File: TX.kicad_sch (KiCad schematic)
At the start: 0 parts

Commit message: Added some little bits and bops
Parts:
- added Q2, Q5: MJD44H11T4G, BR_SOT:TO-252-2_L6.5-W6.1-P4.58-LS10.0-TL, symbol BR_Transistors:BJT_N_MJD44H11T4G
- added Q3, Q4: MJD45H11T4G, BR_SOT:TO-252-2_L6.5-W6.1-P4.58-LS10.0-TL, symbol BR_Transistors:BJT_P_MJD45H11T4G

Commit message: Update TX.kicad_sch
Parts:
- removed Q4: MJD45H11T4G, BR_SOT:TO-252-2_L6.5-W6.1-P4.58-LS10.0-TL, symbol BR_Transistors:BJT_P_MJD45H11T4G
- removed Q5: MJD44H11T4G, BR_SOT:TO-252-2_L6.5-W6.1-P4.58-LS10.0-TL, symbol BR_Transistors:BJT_N_MJD44H11T4G
- Q2: JLCPCB Part Num (none) -> C38780
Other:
- note added: "For collector currents < 1A, these FETs have a current-gain-BW product of around 90MHz For 1A output, we'd need op-amps that can source 10mA"
- note added: "The biasing op amp (using output feedback) needs to have an Enable pin. We want the op amp to enter a high-Z state when not transmitting to avoid driving the BJTs and letting the 1k resistor pull the BJTs off."
- moved on the sheet: Q2, Q3

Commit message: power scheme
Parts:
- added Q4: MJD45H11T4G, BR_SOT:TO-252-2_L6.5-W6.1-P4.58-LS10.0-TL, symbol BR_Transistors:BJT_P_MJD45H11T4G
- added Q5: MJD44H11T4G, BR_SOT:TO-252-2_L6.5-W6.1-P4.58-LS10.0-TL, symbol BR_Transistors:BJT_N_MJD44H11T4G
- Q2: JLCPCB Part Num C38780 -> (none)
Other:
- note removed: "For collector currents < 1A, these FETs have a current-gain-BW product of around 90MHz For 1A output, we'd need op-amps that can source 10mA"
- note removed: "The biasing op amp (using output feedback) needs to have an Enable pin. We want the op amp to enter a high-Z state when not transmitting to avoid driving the BJTs and letting the 1k resistor pull the BJTs off."
- moved on the sheet: Q2, Q3

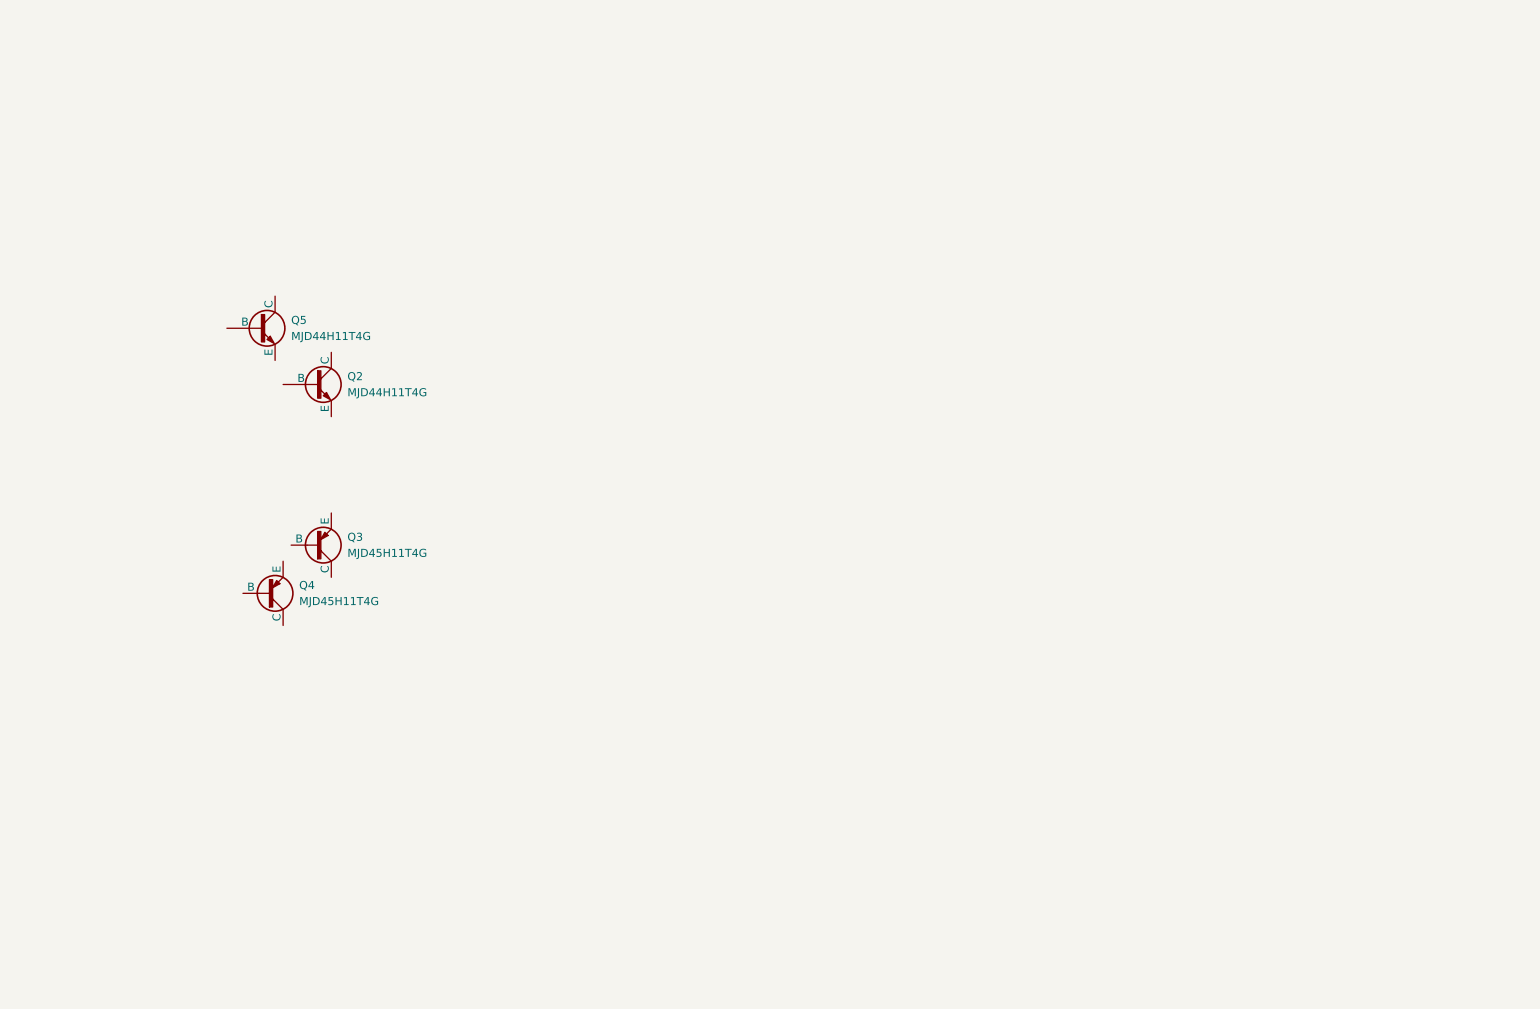
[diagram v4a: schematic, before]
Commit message: Added integrated class ab
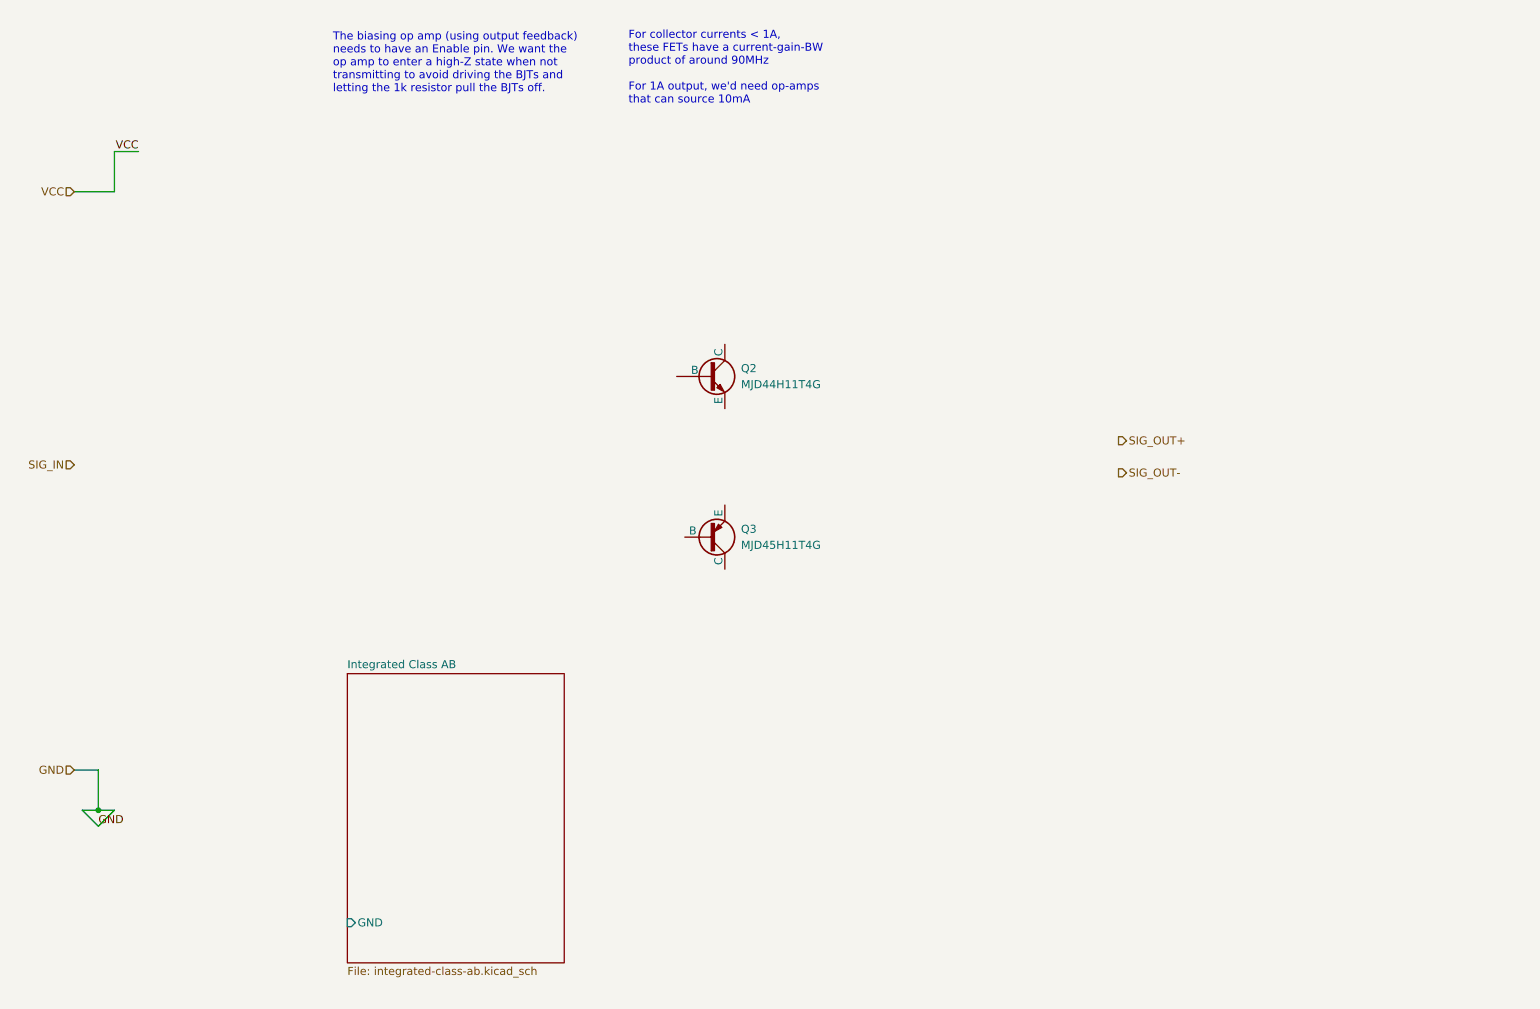
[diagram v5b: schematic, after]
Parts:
- removed Q4: MJD45H11T4G, BR_SOT:TO-252-2_L6.5-W6.1-P4.58-LS10.0-TL, symbol BR_Transistors:BJT_P_MJD45H11T4G
- removed Q5: MJD44H11T4G, BR_SOT:TO-252-2_L6.5-W6.1-P4.58-LS10.0-TL, symbol BR_Transistors:BJT_N_MJD44H11T4G
- Q2: JLCPCB Part Num (none) -> C38780
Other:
- added sheet Integrated Class AB (integrated-class-ab.kicad_sch)
- note added: "For collector currents < 1A, these FETs have a current-gain-BW product of around 90MHz For 1A output, we'd need op-amps that can source 10mA"
- note added: "The biasing op amp (using output feedback) needs to have an Enable pin. We want the op amp to enter a high-Z state when not transmitting to avoid driving the BJTs and letting the 1k resistor pull the BJTs off."
- moved on the sheet: Q2, Q3

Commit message: Added the pin headers to TX, working on a HV line driver design
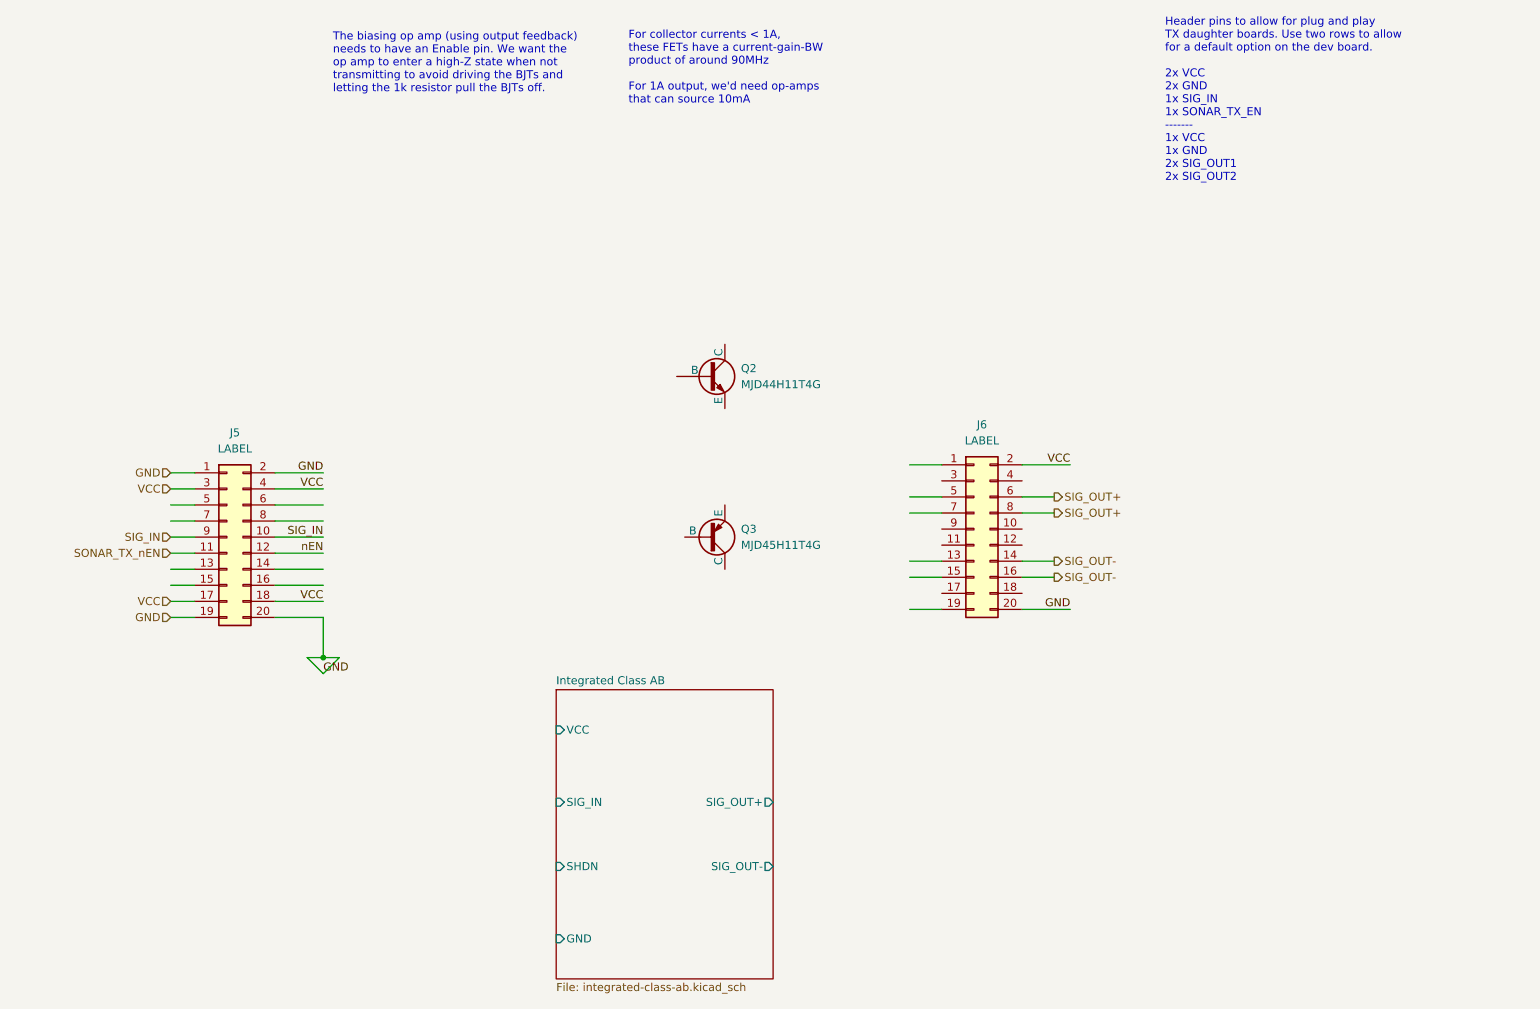
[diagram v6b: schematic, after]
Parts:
- added J5, J6: LABEL, BR_Connectors:HDR-SMD_20P-P2.54-V-M-R2-C10-S7.5, symbol BR_Connectors_Header:Header_Pin_02x10_2.54mm_Vert_PTH
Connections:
- net GND: now also J5.1 (Pin_1), J5.19 (Pin_19), J5.2 (Pin_2), J5.20 (Pin_20), J6.20 (Pin_20)
- net SIG_IN: now also J5.10 (Pin_10), J5.9 (Pin_9)
- net SIG_OUT+: now also J6.6 (Pin_6), J6.8 (Pin_8)
- net SIG_OUT-: now also J6.14 (Pin_14), J6.16 (Pin_16)
- net VCC: now also J5.17 (Pin_17), J5.18 (Pin_18), J5.3 (Pin_3), J5.4 (Pin_4), J6.2 (Pin_2)
- new net SONAR_TX_nEN: J5.11 (Pin_11)
- new net nEN: J5.12 (Pin_12)
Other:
- sheet Integrated Class AB ports: added SHDN, SIG_IN, SIG_OUT+, SIG_OUT-, VCC; removed none
- note added: "Header pins to allow for plug and play TX daughter boards. Use two rows to allow for a default option on the dev board. 2x VCC 2x GND 1x SIG_IN 1x SONAR_TX_EN ------- 1x VCC 1x GND 2x SIG_OUT1 2x SIG_OUT2"

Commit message: Created DAC single-ended to double-ended pre stage for TX path
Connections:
- net 4V: now reaches J5.5 (Pin_5)
- net 4V: now also J5.6 (Pin_6)
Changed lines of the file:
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@@
 		(color 0 0 0 0)
 	)
+	(junction
+		(at 128.27 166.37)
+		(diameter 0)
+		(color 0 0 0 0)
+	)
 	(wire
 		(pts
@@
 	(wire
 		(pts
+			(xy 128.27 127) (xy 128.27 119.38)
+		)
+		(stroke
+			(width 0)
+			(type default)
+		)
+	)
+	(wire
+		(pts
 			(xy 99.06 109.22) (xy 99.06 115.57)
 		)
@@
 	(wire
 		(pts
+			(xy 135.89 160.02) (xy 128.27 160.02)
+		)
+		(stroke
+			(width 0)
+			(type default)
+		)
+	)
+	(wire
+		(pts
 			(xy 214.63 102.87) (xy 209.55 102.87)
 		)
@@
 	(wire
 		(pts
+			(xy 124.46 119.38) (xy 128.27 119.38)
+		)
+		(stroke
+			(width 0)
+			(type default)
+		)
+	)
+	(wire
+		(pts
 			(xy 91.44 96.52) (xy 99.06 96.52)
 		)
@@
 	(wire
 		(pts
+			(xy 125.73 148.59) (xy 135.89 148.59)
+		)
+		(stroke
+			(width 0)
+			(type default)
+		)
+	)
+	(wire
+		(pts
 			(xy 91.44 109.22) (xy 99.06 109.22)
 		)
@@
 	(wire
 		(pts
+			(xy 128.27 166.37) (xy 125.73 166.37)
+		)
+		(stroke
+			(width 0)
+			(type default)
+		)
+	)
+	(wire
+		(pts
 			(xy 191.77 90.17) (xy 196.85 90.17)
 		)
@@
 	(wire
 		(pts
+			(xy 135.89 127) (xy 128.27 127)
+		)
+		(stroke
+			(width 0)
+			(type default)
+		)
+	)
+	(wire
+		(pts
+			(xy 128.27 168.91) (xy 125.73 166.37)
+		)
+		(stroke
+			(width 0)
+			(type default)
+		)
+	)
+	(wire
+		(pts
 			(xy 91.44 101.6) (xy 99.06 101.6)
 		)
@@
 	(wire
 		(pts
+			(xy 125.73 138.43) (xy 135.89 138.43)
+		)
+		(stroke
+			(width 0)
+			(type default)
+		)
+	)
+	(wire
+		(pts
 			(xy 91.44 91.44) (xy 99.06 91.44)
 		)
@@
 	(wire
 		(pts
+			(xy 128.27 160.02) (xy 128.27 166.37)
+		)
+		(stroke
+			(width 0)
+			(type default)
+		)
+	)
+	(wire
+		(pts
 			(xy 91.44 93.98) (xy 99.06 93.98)
 		)
@@
 	(wire
 		(pts
+			(xy 130.81 166.37) (xy 128.27 168.91)
+		)
+		(stroke
+			(width 0)
+			(type default)
+		)
+	)
+	(wire
+		(pts
 			(xy 74.93 86.36) (xy 78.74 86.36)
 		)
@@
 		(pts
 			(xy 96.52 115.57) (xy 99.06 115.57)
+		)
+		(stroke
+			(width 0)
+			(type default)
+		)
+	)
+	(wire
+		(pts
+			(xy 130.81 166.37) (xy 128.27 166.37)
 		)
 		(stroke
@@
 		)
 	)
+	(label "4V"
+		(at 99.06 91.44 180)
+		(effects
+			(font
+				(size 1.27 1.27)
+			)
+			(justify right bottom)
+		)
+	)
 	(label "GND"
 		(at 217.17 107.95 180)
@@
 	)
 	(label "VCC"
+		(at 124.46 119.38 0)
+		(effects
+			(font
+				(size 1.27 1.27)
+			)
+			(justify left bottom)
+		)
+	)
+	(label "VCC"
 		(at 99.06 106.68 180)
 		(effects
@@
 	(label "nEN"
 		(at 99.06 99.06 180)
+		(effects
+			(font
+				(size 1.27 1.27)
+			)
+			(justify right bottom)
+		)
+	)
+	(label "GND"
+		(at 128.27 168.91 180)
 		(effects
 			(font
@@
 		(effects
 			(font
+				(size 1.27 1.27)
+			)
+			(justify right)
+		)
+	)
+	(hierarchical_label "4V"
+		(shape input)
+		(at 74.93 91.44 180)
+		(effects
+			(font

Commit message: shit on a shit stick
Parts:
- added R48: 20k, BR_Passives:R_0201_0603Metric-minimized, symbol BR_Resistors_0201:R_0201_20k
- added R49: 2k, BR_Passives:C_0402_1005Metric-minimized, symbol BR_Resistors_0402:R_0402_2k
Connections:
- net SIG_IN: now also R48.1, R49.1
- net 2x_ATT: now reaches J5.14 (Pin_14)
- net 2x_ATT: now also R48.2
- net 10x_ATT: now reaches J5.16 (Pin_16)
- net 10x_ATT: now also R49.2
- net nEN renamed TX_EN
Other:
- note added: "ATTENUATORS Set 2x LOW to cut signal in half Set 10x LOW to cut signal to 1/10th uses DAC output impedance ~20k"
- moved on the sheet: Q2, Q3
